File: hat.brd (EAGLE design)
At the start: 65 x 56.5 mm, 43 parts, among them U1 ADS1115IDGST, U2 ADXL345, U3 MCP2515-I/SO, U4 MCP2551, X1 16Mhz

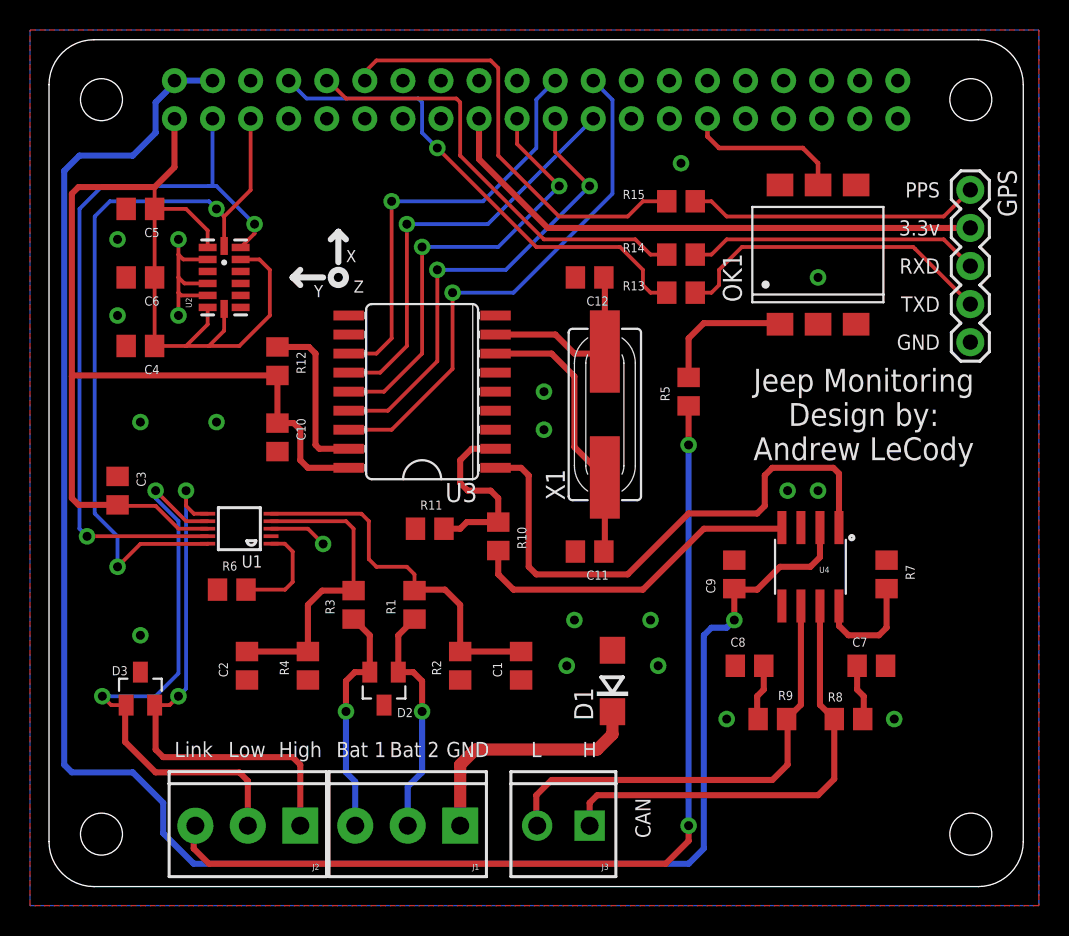
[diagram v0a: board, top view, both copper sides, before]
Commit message: Replaced accelerometer with i2c header
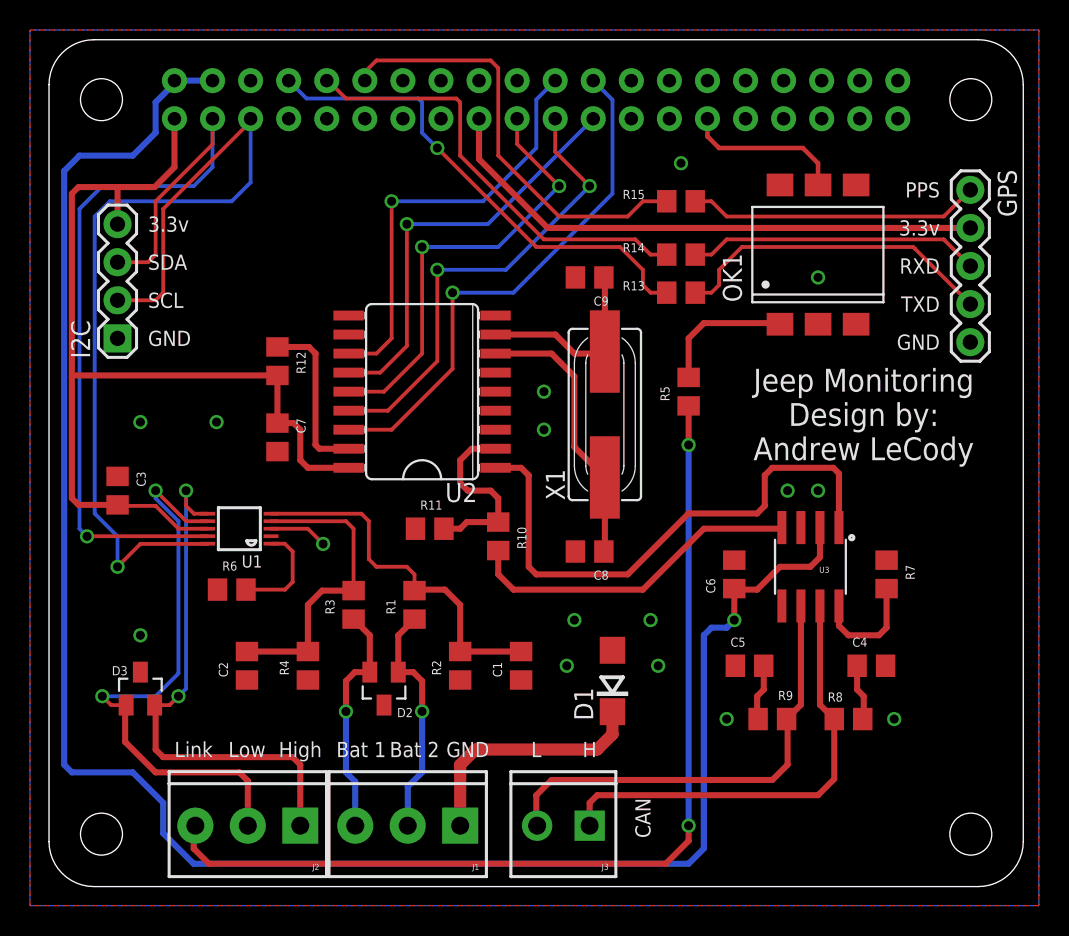
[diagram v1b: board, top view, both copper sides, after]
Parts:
- removed C10: 0.1uF, aceat64-passives:C0805
- removed C11, C12: 22pF, aceat64-passives:C0805
- removed U4: MCP2551, SparkFun-DigitalIC:SO08
- added I2C: (no value), SparkFun-Connectors:1X04
- C4, C5: value 0.1uF -> 560pF
- C6: value 10uF -> 0.1uF
- C7: value 560pF -> 0.1uF
- C8: value 560pF -> 22pF
- C9: value 0.1uF -> 22pF
- U2: value ADXL345 -> MCP2515-I/SO; device SparkFun-Sensors:LGA14 -> mcp2515:SO18L
- U3: value MCP2515-I/SO -> MCP2551; device mcp2515:SO18L -> SparkFun-DigitalIC:SO08
- moved C4 53.2 mm to (54.9, 14.7), turned to 0 degrees
- moved C5 50.8 mm to (46.7, 14.7)
- moved C6 44.3 mm to (45.7, 20.8), turned to 90 degrees
- moved C7 42.5 mm to (15.2, 30.0), turned to 270 degrees
- moved U3 28.4 mm to (50.8, 21.3), turned to 180 degrees
- moved C9 22.0 mm to (36.1, 40.6), turned to 180 degrees
- moved U2 15.2 mm to (24.9, 33.0)
- moved C8 13.1 mm to (36.1, 22.4)
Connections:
- net 3.3V: now also C7.1, I2C.4, U2.18; no longer C10.1, C4.1, C5.1, C6.1, U2.1, U2.12, U2.6, U2.7, U3.18
- net 5V: now also C6.1, U3.2; no longer C9.1, U4.2
- net CANH: now also U3.7; no longer U4.7
- net CANL: now also U3.6; no longer U4.6
- net GND: now also I2C.1, U2.9, U3.3; no longer C10.2, C11.2, C12.2, U2.2, U2.4, U2.5, U3.9, U4.3
- net GPIO25: now also U2.12; no longer U3.12
- net N$14: now also C9.1, U2.8; no longer C12.1, U3.8
- net N$15: now also C8.1, U2.7; no longer C11.1, U3.7
- net N$4: now also U2.2; no longer U3.2
- net N$6: now also C4.1; no longer C7.1
- net N$8: now also C5.1; no longer C8.1
- net RS: now also U3.8; no longer U4.8
- net RXCAN: now also U3.4; no longer U4.4
- net SCL: now also I2C.2; no longer U2.14
- net SDA: now also I2C.3; no longer U2.13
- net SPI_CE0: now also U2.16; no longer U3.16
- net SPI_MISO: now also U2.15; no longer U3.15
- net SPI_MOSI: now also U2.14; no longer U3.14
- net SPI_SCLK: now also U2.13; no longer U3.13
- net TXCAN: now also U2.1; no longer U4.1
- net U5_RST: now also U2.17; no longer U3.17
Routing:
- net 3.3V: track 138.3 -> 105.0 mm
- net SCL: track 49.4 -> 63.5 mm, vias 2 -> 1
- net GND: track 15.2 -> 3.90 mm, vias 20 -> 16
- net SDA: track 49.9 -> 56.8 mm, vias 2 -> 1
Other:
- board text added: "SCL"
- board text added: "SDA"
- board text removed: "X"
- board text removed: "Y"
- board text removed: "Z"

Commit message: Rename U5_RST to U2_RST
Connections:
- net U5_RST renamed U2_RST
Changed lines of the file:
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@@
 <wire x1="27.874" y1="24.318" x2="29.972" y2="24.318" width="0.4064" layer="1"/>
 </signal>
-<signal name="U5_RST">
+<signal name="U2_RST">
 <contactref element="R12" pad="1"/>
 <contactref element="U2" pad="17"/>
